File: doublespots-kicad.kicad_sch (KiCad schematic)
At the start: 9 parts

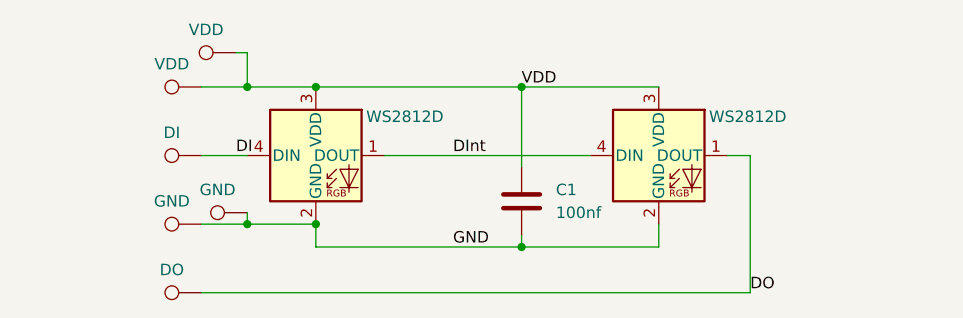
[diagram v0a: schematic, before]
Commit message: Update PCB with connectors and ground plane
This change also adds a ground plane and reworks some routing.

Signed-off-by: Markus Hutzler <markus.hutzler@me.com>
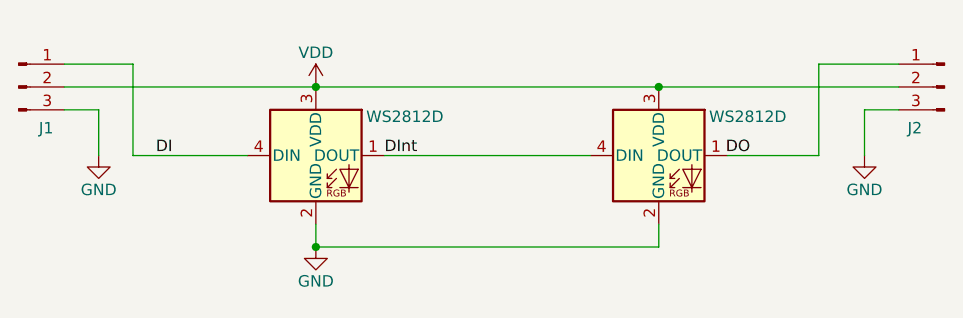
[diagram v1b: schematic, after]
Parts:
- removed C1: 100nf, Capacitor_SMD:C_1206_3216Metric, symbol Device:C
- removed DI1: DI, MyLibrary:TestPoint_Pad_2.4x1.6mm, symbol Connector:TestPoint
- removed DO1: DO, MyLibrary:TestPoint_Pad_2.4x1.6mm, symbol Connector:TestPoint
- removed GND1, GND2: GND, MyLibrary:TestPoint_Pad_2.4x1.6mm, symbol Connector:TestPoint
- removed VDD1, VDD2: VDD, MyLibrary:TestPoint_Pad_2.4x1.6mm, symbol Connector:TestPoint
- added J1, J2: Conn_01x03_Pin, MyLibrary:con_1x03_solder, symbol Connector:Conn_01x03_Pin
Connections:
- net DI: now also J1.1 (Pin_1)
- net DO: now also J2.1 (Pin_1)
- net GND: now also J1.3 (Pin_3), J2.3 (Pin_3)
- net VDD: now also J1.2 (Pin_2), J2.2 (Pin_2)
